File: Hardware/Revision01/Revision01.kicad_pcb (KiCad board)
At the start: 4 copper layers, 100 x 110.1 mm, 96 parts, among them J1 CANBUS backup, J10 StrainConn, J12 Conn_01x02, J13 Conn_01x02, J2 Battery connector, J3 StrainConn, J4 StrainConn, J5 StrainConn, J6 StrainConn, J7 StrainConn, J8 StrainConn, J9 StrainConn, Q1 PMOS, Q2 NMOS, Q3 PMOS, SW1 ON/OFF_SW_SPST_LED, U1 NUCLEO-L476RG, U2 MRF89XAM9AT-I/RM

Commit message: COMPONENT LAYOUT COMPLETE
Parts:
- removed J13: Conn_01x02, Connector_PinHeader_2.54mm:PinHeader_1x02_P2.54mm_Vertical
- added J11: StrainConn, JST_3PIN:JST_B3B-XH-A, F.Cu at (202.3, 89.8)
- added U3: ICM-45605, ICM-45605:XDCR_ICM-45605, B.Cu at (160.2, 97.4)
- C10, C11, C12, C13, C3, C4, C5, C6, C7, C8, C9, D1, D10, D11, D12, D13, D14, D15, D16, D3, D4, D7, D8, D9, F2, F3, F4, F5, F6, F7, F8, F9, FID1, FID2, FID3, Q1, Q2, Q3, R1, R10, R12, R14, R16, R17, R26, R27, R28, R29, R3, R5, R7, TP1, TP10, TP2, TP3, TP4, TP5, TP6, TP7, TP8, TP9: moved to B.Cu
- J10, J5, J6, J7, J8, J9, SW1, U1, U2: moved to F.Cu
- J12: value Conn_01x02 -> StrainConn; footprint Connector_PinHeader_2.54mm:PinHeader_1x02_P2.54mm_Vertical -> JST_3PIN:JST_B3B-XH-A
- J2: value Battery connector -> Conn_01x02; footprint Connector_JST:JST_PH_B2B-PH-K_1x02_P2.00mm_Vertical -> Connector_PinHeader_2.54mm:PinHeader_1x02_P2.54mm_Vertical; moved to F.Cu
- J3: value StrainConn -> Conn_01x02; footprint JST_3PIN:JST_B3B-XH-A -> Connector_PinHeader_2.54mm:PinHeader_1x02_P2.54mm_Vertical; moved to F.Cu
- J4: value StrainConn -> Battery connector; footprint JST_3PIN:JST_B3B-XH-A -> Connector_JST:JST_PH_B2B-PH-K_1x02_P2.00mm_Vertical; moved to F.Cu
- R11, R13, R15, R9: value 1.6K +-1% -> 1M +-1%; moved to B.Cu
- R2, R4, R6, R8: value 1M +-1% -> 1.6K +-1%; moved to B.Cu
- moved F6 228.1 mm to (204.6, 114.9), turned to 180 degrees
- moved F7 221.6 mm to (204.6, 102.3), turned to 180 degrees
- moved J1 215.9 mm to (192.3, 137.4)
- moved F8 215.4 mm to (204.9, 87.2), turned to 180 degrees
- moved F9 210.8 mm to (204.7, 75.2), turned to 180 degrees
- moved J12 198.0 mm to (202.3, 77.7), turned to -90 degrees
- moved C6 175.8 mm to (188.5, 123.0), turned to 180 degrees
- moved R5 175.4 mm to (198.8, 117.3)
- moved R6 172.6 mm to (198.8, 104.7)
- moved C7 171.8 mm to (187.3, 117.2), turned to 90 degrees
- moved D10 171.7 mm to (188.0, 127.2), turned to 180 degrees
- moved D9 170.3 mm to (185.9, 120.6), turned to 0 degrees
- moved R7 167.2 mm to (198.5, 89.7)
- moved R8 166.3 mm to (198.8, 77.7)
- moved C8 165.7 mm to (187.3, 91.4), turned to -90 degrees
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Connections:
- C1 pad 1: Net-(J2-Pin_2) -> Net-(J4-Pin_2)
- C14 pad 2: GND -> /PB14_SPI2_MISO
- C15 pad 2: GND -> /PB14_SPI2_MISO
- C2 pad 1: /AIN1_8 -> /AIN1_1
- C3 pad 1: /AIN1_7 -> /AIN1_2
- C4 pad 1: /AIN1_11 -> /AIN1_7
- C5 pad 1: /AIN1_10 -> /AIN1_6
- C6 pad 1: /AIN1_1 -> /AIN1_8
- C7 pad 1: /AIN1_2 -> /AIN1_5
- C8 pad 1: /AIN1_5 -> /AIN1_11
- C9 pad 1: /AIN1_6 -> /AIN1_10
- D1 pad 2: /AIN1_8 -> /AIN1_1
- D10 pad 1: /AIN1_1 -> /AIN1_8
- D11 pad 2: /AIN1_2 -> /AIN1_5
- D12 pad 1: /AIN1_2 -> /AIN1_5
- D13 pad 2: /AIN1_5 -> /AIN1_11
- D14 pad 1: /AIN1_5 -> /AIN1_11
- D15 pad 2: /AIN1_6 -> /AIN1_10
- D16 pad 1: /AIN1_6 -> /AIN1_10
- D2 pad 1: /AIN1_8 -> /AIN1_1
- D3 pad 2: /AIN1_7 -> /AIN1_2
- D4 pad 1: /AIN1_7 -> /AIN1_2
- D5 pad 2: /AIN1_11 -> /AIN1_7
- D6 pad 1: /AIN1_11 -> /AIN1_7
- D7 pad 2: /AIN1_10 -> /AIN1_6
- D8 pad 1: /AIN1_10 -> /AIN1_6
- D9 pad 2: /AIN1_1 -> /AIN1_8
- F2 pad 2: Net-(F2-Pad2) -> Net-(J5-Pin_3)
- F3 pad 2: Net-(F3-Pad2) -> Net-(J6-Pin_3)
- F4 pad 2: Net-(F4-Pad2) -> Net-(J7-Pin_3)
- F5 pad 2: Net-(F5-Pad2) -> Net-(J8-Pin_3)
- F6 pad 2: Net-(F6-Pad2) -> Net-(J9-Pin_3)
- F7 pad 2: Net-(F7-Pad2) -> Net-(J10-Pin_3)
- F9 pad 2: Net-(F9-Pad2) -> Net-(J12-Pin_3)
- J10 pad 2: /Application/OpAmpOutput8 -> /Application/OpAmpOutput6
- J10 pad 3: /Application/+StrainV -> Net-(J10-Pin_3)
- J12 pad 1: unconnected-(J12-Pin_1-Pad1) -> GND
- J12 pad 2: unconnected-(J12-Pin_2-Pad2) -> /Application/OpAmpOutput8
- J4 pad 2: /Application/OpAmpOutput2 -> Net-(J4-Pin_2)
- J5 pad 2: /Application/OpAmpOutput3 -> /Application/OpAmpOutput1
- J5 pad 3: /Application/+StrainV -> Net-(J5-Pin_3)
- J6 pad 2: /Application/OpAmpOutput4 -> /Application/OpAmpOutput2
- J6 pad 3: /Application/+StrainV -> Net-(J6-Pin_3)
- J7 pad 2: /Application/OpAmpOutput5 -> /Application/OpAmpOutput3
- J7 pad 3: /Application/+StrainV -> Net-(J7-Pin_3)
- J8 pad 2: /Application/OpAmpOutput6 -> /Application/OpAmpOutput4
- J8 pad 3: /Application/+StrainV -> Net-(J8-Pin_3)
- J9 pad 2: /Application/OpAmpOutput7 -> /Application/OpAmpOutput5
- J9 pad 3: /Application/+StrainV -> Net-(J9-Pin_3)
- R1 pad 2: /AIN1_8 -> /AIN1_1
- R10 pad 1: /AIN1_1 -> /AIN1_2
- R11 pad 1: /Application/OpAmpOutput6 -> /AIN1_7
- R11 pad 2: /AIN1_2 -> GND
- R12 pad 1: /AIN1_2 -> /AIN1_6
- R13 pad 1: /Application/OpAmpOutput7 -> /AIN1_8
- R13 pad 2: /AIN1_5 -> GND
- R15 pad 1: /Application/OpAmpOutput8 -> /AIN1_11
- R15 pad 2: /AIN1_6 -> GND
- R16 pad 1: /AIN1_6 -> /AIN1_10
- R2 pad 1: /AIN1_8 -> /Application/OpAmpOutput2
- R2 pad 2: GND -> /AIN1_2
- R3 pad 1: /Application/OpAmpOutput2 -> /Application/OpAmpOutput3
- R4 pad 1: /AIN1_7 -> /Application/OpAmpOutput4
- R4 pad 2: GND -> /AIN1_6
- R5 pad 1: /Application/OpAmpOutput3 -> /Application/OpAmpOutput5
- R5 pad 2: /AIN1_11 -> /AIN1_8
- R6 pad 1: /AIN1_11 -> /Application/OpAmpOutput6
- R6 pad 2: GND -> /AIN1_5
- R7 pad 1: /Application/OpAmpOutput4 -> /Application/OpAmpOutput7
- R7 pad 2: /AIN1_10 -> /AIN1_11
- R8 pad 1: /AIN1_10 -> /Application/OpAmpOutput8
- R8 pad 2: GND -> /AIN1_10
- R9 pad 1: /Application/OpAmpOutput5 -> /AIN1_1
- R9 pad 2: /AIN1_1 -> GND
- SW1 pad 2: Net-(J2-Pin_2) -> Net-(J4-Pin_2)
- U1 pad CN10_30: /PB13_SPI2_SCK -> /PB14_SPI2_MISO
- U1 pad CN10_35: /AIN1_7 -> /AIN1_5
- U1 pad CN7_30: /AIN1_5 -> /AIN1_7
- U2 pad 1: GND -> /PB14_SPI2_MISO
- U2 pad 11: GND -> /PB14_SPI2_MISO
- U2 pad 12: GND -> /PB14_SPI2_MISO
- U2 pad 6: /PB13_SPI2_SCK -> /PB14_SPI2_MISO
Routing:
- net /Application/+StrainV: track 0.00 -> 254.5 mm
- net /PB14_SPI2_MISO: track 0.00 -> 109.2 mm
- net /AIN1_6: track 0.00 -> 47.1 mm
- net /AIN1_5: track 0.00 -> 27.8 mm
- net /AIN1_2: track 0.00 -> 27.7 mm
- net /AIN1_10: track 0.00 -> 24.6 mm
- net /PB15_SPI2_MOSI: track 0.00 -> 24.3 mm
- net /AIN1_8: track 0.00 -> 20.3 mm
- net /AIN1_11: track 0.00 -> 18.2 mm
- net GND: track 0.00 -> 12.8 mm, vias 0 -> 11
- net Net-(J4-Pin_2): track 0.00 -> 11.1 mm
- net /AIN1_1: track 0.00 -> 10.5 mm
- net /AIN1_7: track 0.00 -> 9.59 mm
- net Net-(SW1-A): track 0.00 -> 5.63 mm
- net Net-(Q2-D): track 0.00 -> 4.14 mm
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- added copper zone on B.Cu, net /AIN1_1
- added copper zone on F.Cu, net GND

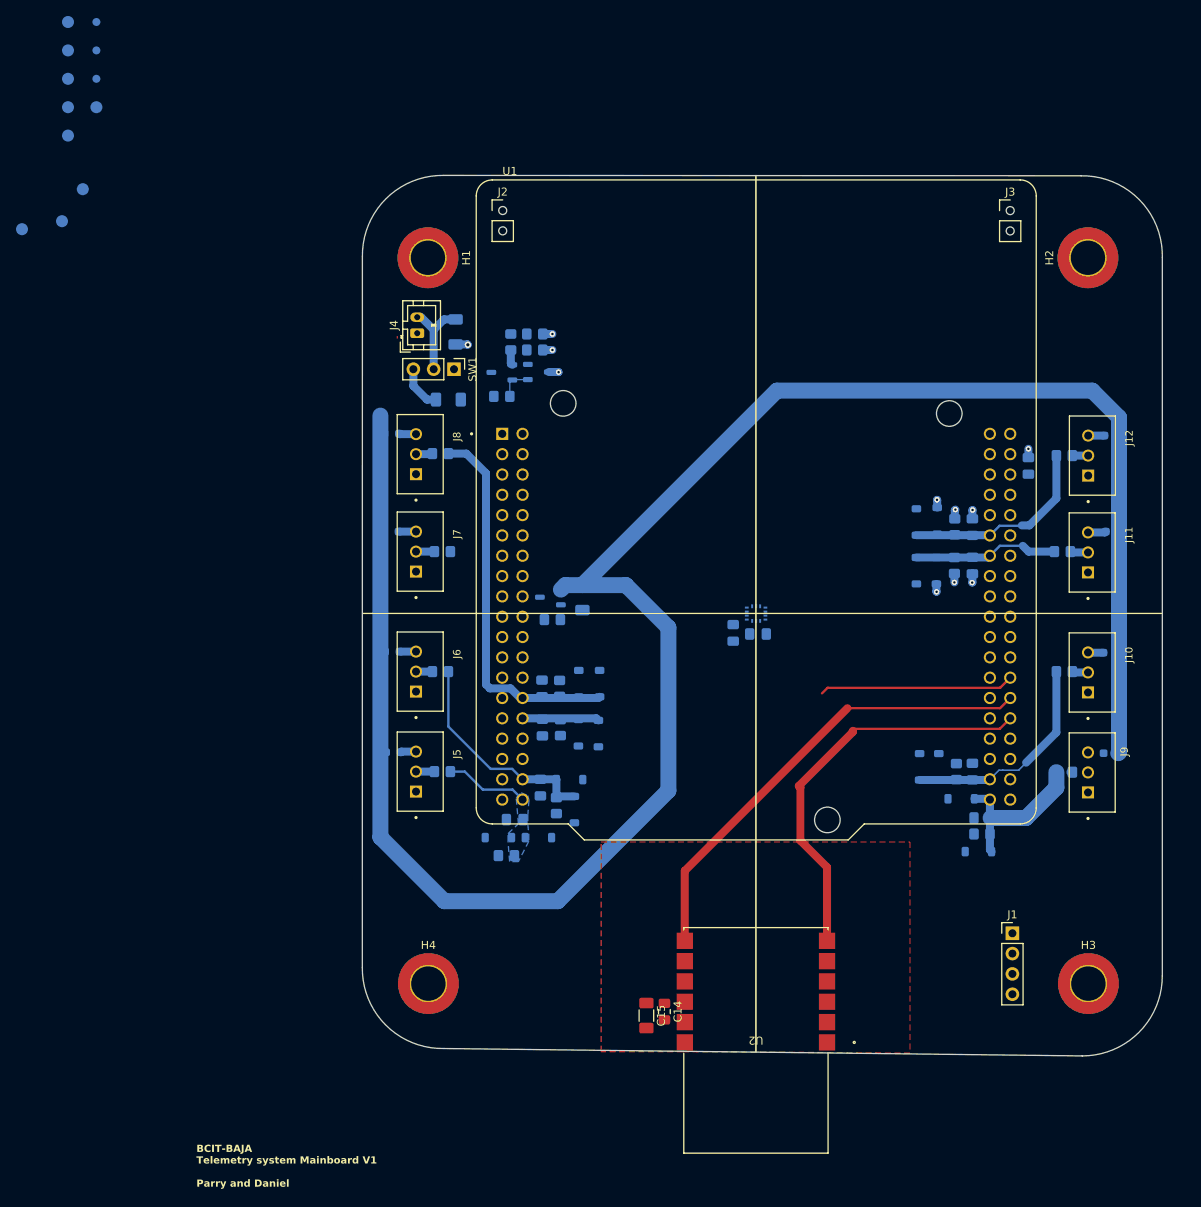
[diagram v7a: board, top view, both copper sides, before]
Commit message: FINISHED most of PCB ROUTING. Awaiting feedback to ensure no coupling between power and analog. Have yet to put stitching VIA's
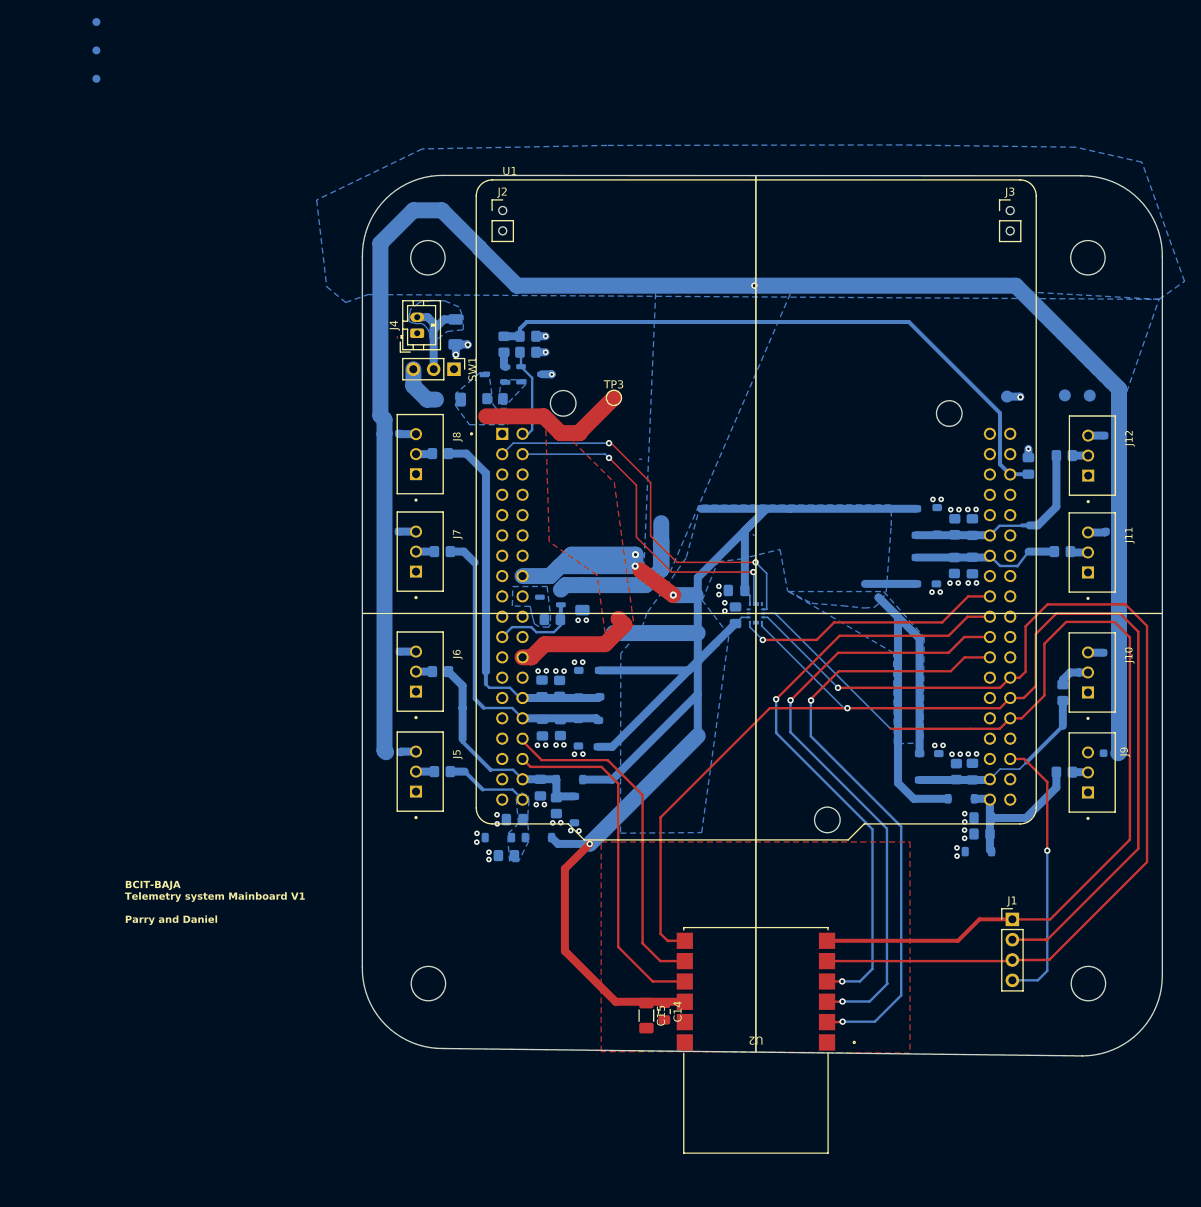
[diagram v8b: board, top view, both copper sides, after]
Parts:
- removed TP1, TP2, TP4, TP5, TP6, TP7: TestPoint, TestPoint:TestPoint_Pad_D1.5mm
- H1, H2, H3, H4: value MountingHole_Pad_MP -> MountingHole; footprint MountingHole:MountingHole_4.3mm_M4_ISO7380_Pad_TopBottom -> MountingHole:MountingHole_4.3mm_M4
- TP3: moved to F.Cu
- moved TP9 132.0 mm to (198.8, 70.2)
- moved TP8 120.1 mm to (191.6, 70.3)
- moved TP10 88.7 mm to (201.9, 70.2)
- moved TP3 82.8 mm to (142.5, 70.5), turned to 0 degrees
- moved C12 5.32 mm to (157.8, 94.5), turned to 180 degrees
- moved C11 3.66 mm to (157.7, 97.6), turned to 90 degrees
- moved R6 2.64 mm to (198.6, 107.3), turned to -90 degrees
- moved J1 1.74 mm to (192.3, 135.7)
- moved R28 0.90 mm to (128.7, 63.8)
- moved R29 0.90 mm to (131.7, 62.8)
- moved Q2 0.90 mm to (132.2, 67.5)
- moved R26 0.90 mm to (131.7, 64.8)
- moved Q3 0.90 mm to (127.6, 67.6)
- moved R27 0.90 mm to (127.6, 70.6)
- turned U3 to 90 degrees
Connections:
- C14 pad 2: /PB14_SPI2_MISO -> GND
- C15 pad 2: /PB14_SPI2_MISO -> GND
- U1 pad CN10_18: /USB_5V_GPIO_EN -> unconnected-(U1B-PB11-PadCN10_18)
- U1 pad CN10_27: /~{CANBUS_CS_GPIO} -> unconnected-(U1B-PB4-PadCN10_27)
- U1 pad CN10_30: /PB14_SPI2_MISO -> /PB13_SPI2_SCK
- U1 pad CN10_34: unconnected-(U1B-PC4-PadCN10_34) -> /~{CANBUS_CS_GPIO}
- U1 pad CN10_8: +5V_USB -> unconnected-(U1B-U5V-PadCN10_8)
- U1 pad CN7_17: /ANT_CSDATA_GPIO -> unconnected-(U1A-PA15-PadCN7_17)
- U1 pad CN7_21: /ANT_IRQ1_GPIO -> /StrainV_Enable_GPIO
- U1 pad CN7_32: unconnected-(U1A-PA4-PadCN7_32) -> /ANT_CSDATA_GPIO
- U1 pad CN7_34: unconnected-(U1A-PB0-PadCN7_34) -> /ANT_IRQ1_GPIO
- U1 pad CN7_35: /StrainV_Enable_GPIO -> unconnected-(U1A-PC2-PadCN7_35)
- U1 pad CN7_7: Net-(U1A-BOOT0) -> unconnected-(U1A-BOOT0-PadCN7_7)
- U2 pad 1: /PB14_SPI2_MISO -> GND
- U2 pad 11: /PB14_SPI2_MISO -> GND
- U2 pad 12: /PB14_SPI2_MISO -> GND
- U2 pad 6: /PB14_SPI2_MISO -> /PB13_SPI2_SCK
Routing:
- net +3.3V: track 0.00 -> 293.8 mm, vias 0 -> 4
- net /PB13_SPI2_SCK: track 0.00 -> 130.4 mm
- net /PB15_SPI2_MOSI: track 24.3 -> 135.0 mm, vias 0 -> 1
- net /PC5_AIN2_14_BATT_V: track 0.00 -> 78.5 mm
- net /ANT_CSCON_GPIO: track 0.00 -> 77.1 mm, vias 0 -> 2
- net /ANT_RESET_ANT_GPIO: track 0.00 -> 76.9 mm, vias 0 -> 2
- net /ANT_IRQ0_GPIO: track 0.00 -> 76.0 mm, vias 0 -> 2
- net /ICM_CS_GPIO: track 0.00 -> 49.2 mm, vias 0 -> 2
- net /PB14_SPI2_MISO: track 109.2 -> 156.2 mm, vias 0 -> 1
- net /ANT_IRQ1_GPIO: track 0.00 -> 43.8 mm
- net /ICM_INT2_GPIO: track 0.00 -> 42.9 mm, vias 0 -> 2
- net /ANT_CSDATA_GPIO: track 0.00 -> 42.8 mm
- net /~{CANBUS_CS_GPIO}: track 0.00 -> 34.3 mm, vias 0 -> 1
- net +V_batt: track 0.00 -> 34.2 mm
- net /ICM_INT1_GPIO: track 0.00 -> 33.5 mm, vias 0 -> 1
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- added copper zone on B.Cu, net +3.3V
- added copper zone on B.Cu, net +5V
- added copper zone on B.Cu, net +V_batt
- added copper zone on F.Cu, net +V_batt
- added copper zone on B.Cu, net /Application/+StrainV
- added copper zone on B.Cu, net Net-(J4-Pin_2)
- added copper zone on B.Cu, net Net-(Q2-D)
